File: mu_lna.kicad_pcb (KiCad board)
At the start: 2 copper layers, 100 x 76.8 mm, 60 parts, among them J1 Conn_01x02, J2 Conn_01x02, J3 Conn_01x02, J4 Conn_01x02, J5 Conn_01x01, U1 ADA4523-1, U2 Opamp_Dual_Generic, U3 ADA4523-1, U4 ADA4523-1, U5 ADA4523-1

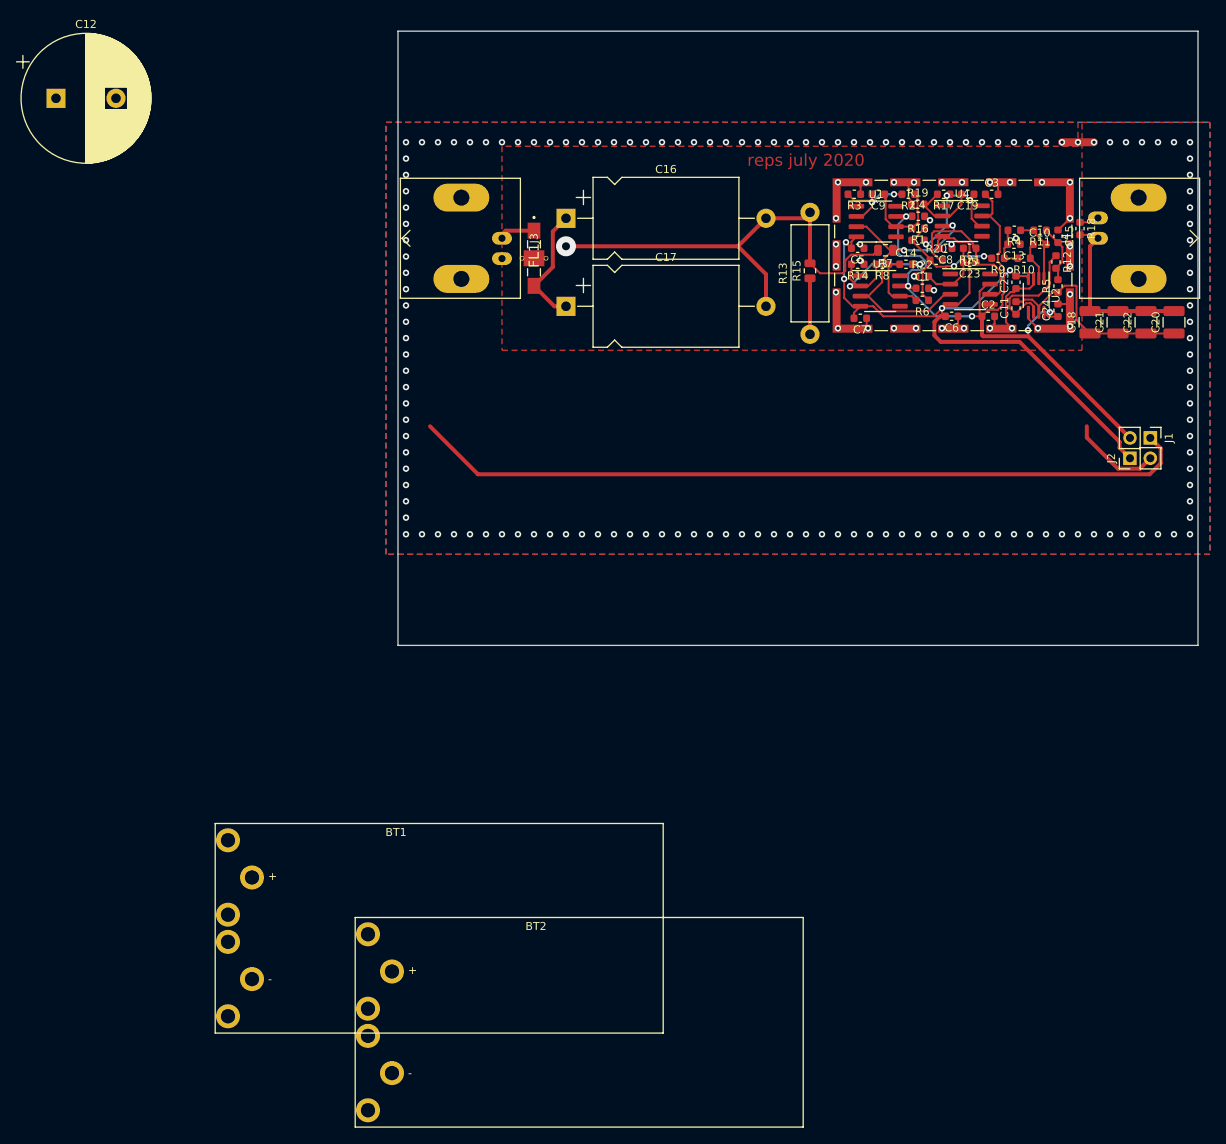
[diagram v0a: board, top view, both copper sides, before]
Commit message: new layout for Bopla 84080100
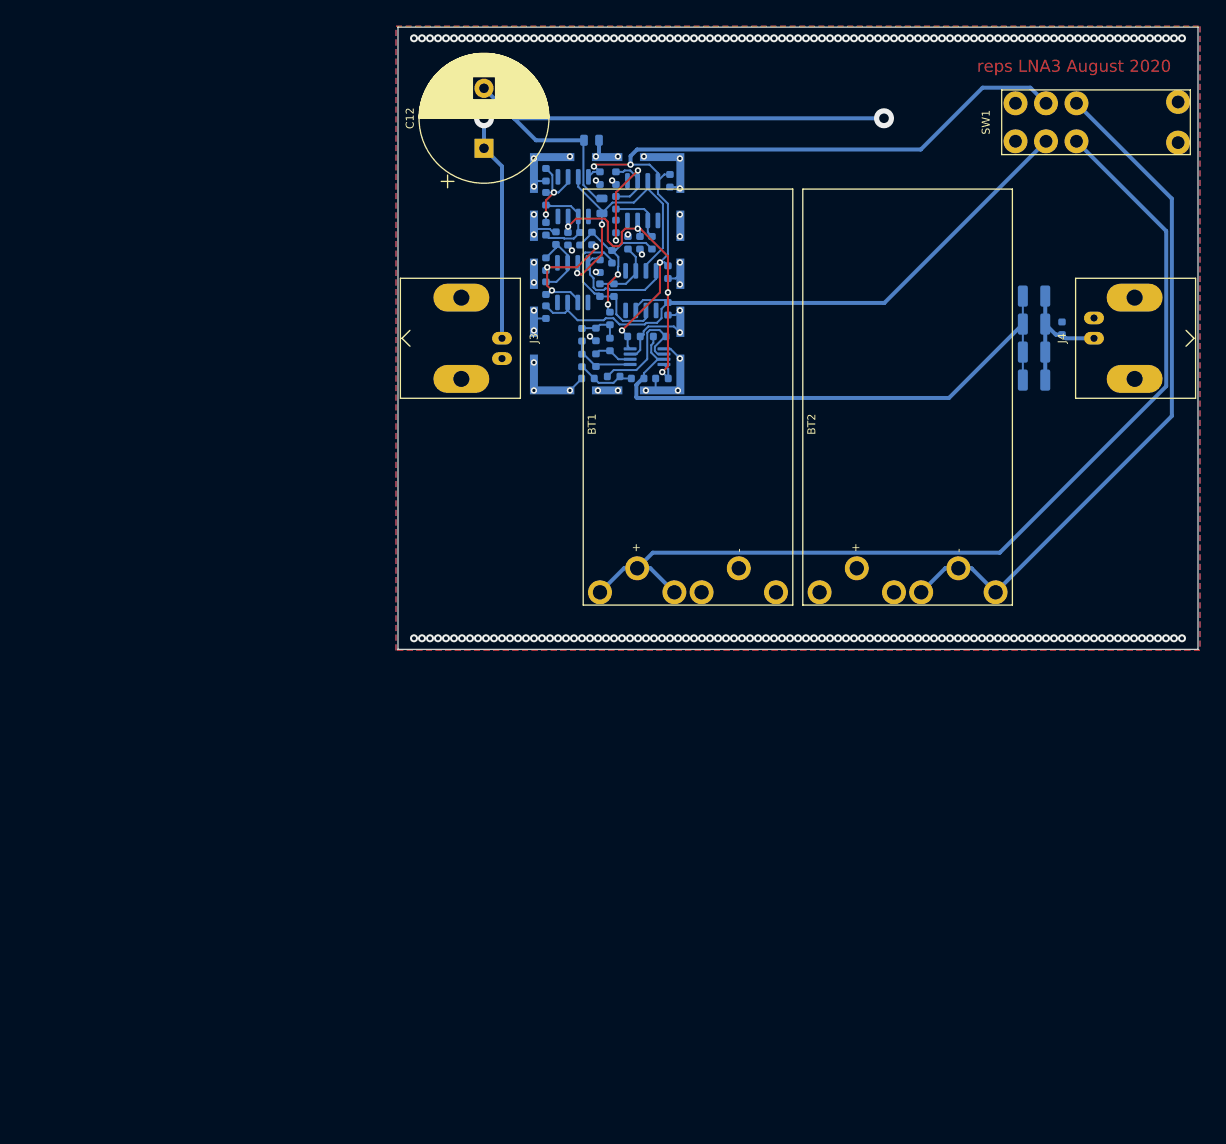
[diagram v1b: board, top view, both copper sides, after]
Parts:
- removed C16, C17: 477µF, Capacitor_THT:CP_Axial_L18.0mm_D10.0mm_P25.00mm_Horizontal
- removed FL1: NFE61PT102E1H9L, SamacSys_Parts:NFE61
- removed J1, J2: Conn_01x02, Connector_PinHeader_2.54mm:PinHeader_1x02_P2.54mm_Vertical
- removed R13: 2kOhm, Resistor_THT:R_Axial_DIN0414_L11.9mm_D4.5mm_P15.24mm_Horizontal
- added SW1: SWW246/7, my_lib:RS_DPDT, F.Cu at (176.0, 73.0)
- C1, C10, C11, C13, C14, C15, C18, C19, C2, C20, C21, C22, C23, C24, C25, C3, C4, C5, C6, C7, C8, C9, J5, R1, R10, R11, R12, R14, R15, R16, R17, R18, R19, R2, R20, R21, R22, R3, R4, R5, R6, R7, R8, R9, U1, U2, U3, U4, U5: moved to B.Cu
- moved BT2 88.0 mm to (158.7, 110.8), turned to 90 degrees
- moved BT1 72.8 mm to (131.2, 110.8), turned to 90 degrees
- moved C15 61.4 mm to (118.7, 105.0), turned to 0 degrees
- moved R11 59.5 mm to (118.0, 102.8), turned to 90 degrees
- moved C3 57.6 mm to (113.5, 96.7), turned to 270 degrees
- moved C10 57.3 mm to (119.7, 102.7), turned to 270 degrees
- moved R12 57.1 mm to (122.0, 104.8), turned to 0 degrees
- moved R4 55.6 mm to (118.0, 99.6), turned to 90 degrees
- moved C19 54.0 mm to (113.5, 93.7), turned to 90 degrees
- moved C12 53.9 mm to (105.8, 76.2), turned to 90 degrees
- moved R5 53.8 mm to (125.0, 105.0), turned to 180 degrees
- moved C13 53.5 mm to (119.7, 99.5), turned to 90 degrees
- moved R10 52.9 mm to (121.5, 100.8), turned to 90 degrees
- moved R17 50.5 mm to (113.5, 90.7), turned to 90 degrees
- moved C24 50.2 mm to (128.0, 105.0), turned to 180 degrees
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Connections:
- J3 pad 1: Net-(FL1-Pad1) -> Net-(C12-Pad1)
- R15 pad 1: GND -> Net-(C12-Pad2)
- R15 pad 2: Net-(C12-Pad2) -> GND
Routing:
- net Net-(BT2-Pad2): track 11.5 -> 87.0 mm, vias 1 -> 0
- net Net-(C11-Pad2): track 27.2 -> 72.9 mm
- net +12V: track 87.3 -> 122.1 mm, vias 5 -> 4
- net Net-(BT1-Pad1): track 98.1 -> 122.6 mm
- net -12V: track 90.4 -> 113.2 mm
- net GND: track 49.3 -> 35.0 mm, vias 180 -> 229
- net Net-(C12-Pad1): track 15.9 -> 28.4 mm, vias 0 -> 1
- net Net-(C12-Pad2): track 58.5 -> 70.1 mm
- net Net-(C18-Pad2): track 22.4 -> 17.3 mm
- net Net-(FL1-Pad1): track 4.19 -> 0.00 mm
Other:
- board size 100 x 76.8 mm -> 100 x 77.8 mm
- board text added: "reps LNA3 August 2020"
- board text removed: "reps july 2020"
